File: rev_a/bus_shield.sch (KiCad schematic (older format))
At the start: 42 parts, among them J1 TERMINATE_JUMPER, SW1 MJTP1243, U1 74HCT08, U2 LM2940, U3 MCP2562, U4 LM117T-3.3, U5 ATMEGA328_DIP28, X1 16MHz

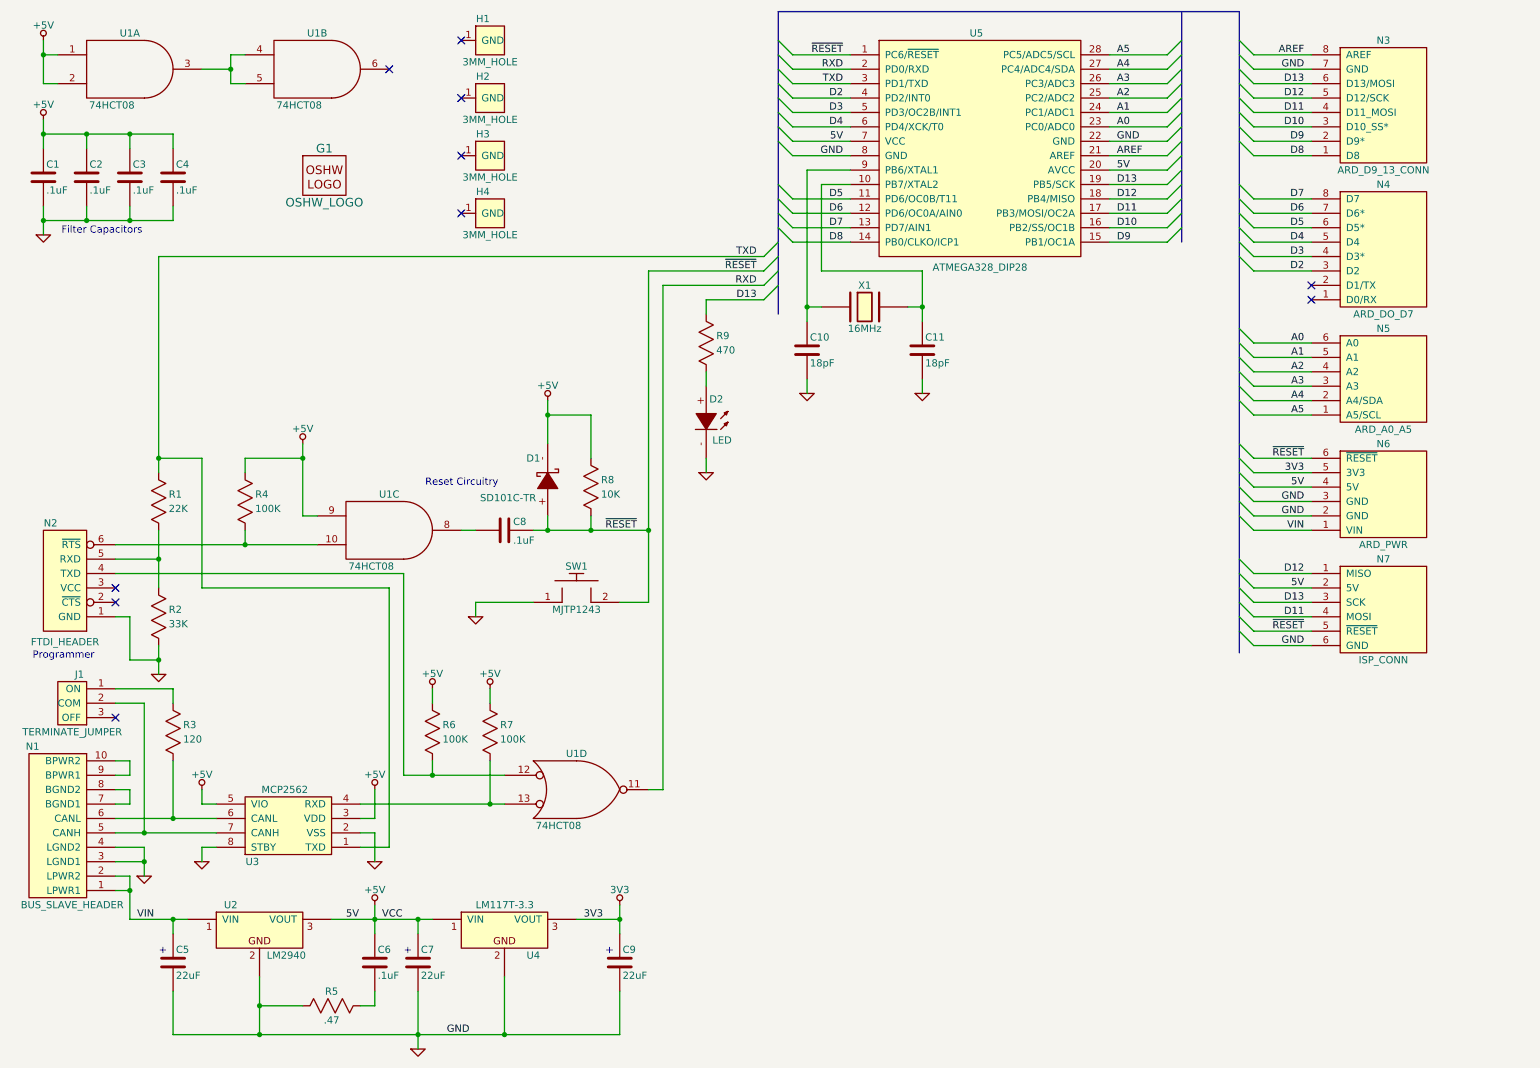
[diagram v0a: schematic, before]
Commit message: Reset from bus circuit.
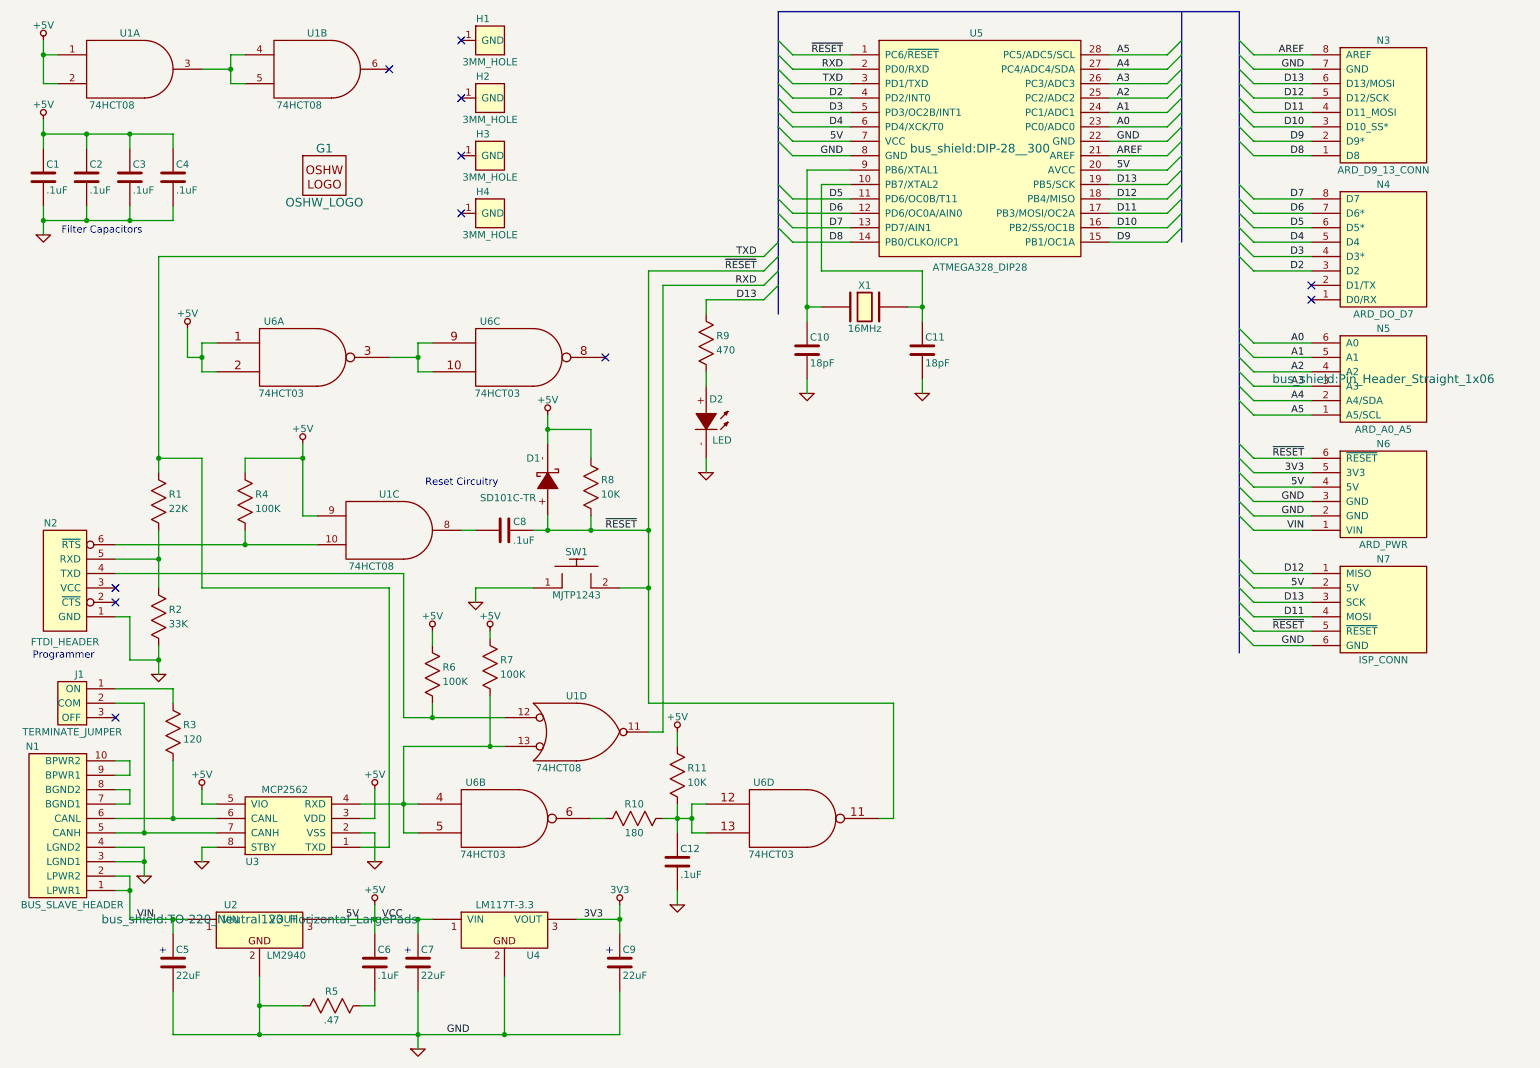
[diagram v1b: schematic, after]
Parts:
- added C12: .1uF, bus_shield:Capacitor3MMDiscRM2.5, symbol C_VERT
- added R10: 180, bus_shield:Resistor_Horizontal_400, symbol R_HORIZ
- added R11: 10K, bus_shield:Resistor_Horizontal_400, symbol R_VERT
- added U6: 74HCT03, bus_shield:DIP-14__300, symbol 74xx00
- N5: footprint ~ -> bus_shield:Pin_Header_Straight_1x06
- U2: footprint ~ -> bus_shield:TO-220_Neutral123_Horizontal_LargePads
- U5: footprint ~ -> bus_shield:DIP-28__300
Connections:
- net +5V: now also R11.2, U6.1, U6.14 (VCC), U6.14 (VCC), U6.14 (VCC), U6.14 (VCC), U6.2
- net GND: now also C12.2, U6.7 (GND), U6.7 (GND), U6.7 (GND), U6.7 (GND)
- net ~RESET: now also U6.11
- net at R7.1, U1.13, U3.4 (RXD): now also U6.4, U6.5
- new net: R10.1, U6.6
- new net: C12.1, R10.2, R11.1, U6.12, U6.13
- new net: U6.10, U6.3, U6.9
- no-connect marks 10 -> 11
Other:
- moved on the sheet: R6, R7, SW1, U1D

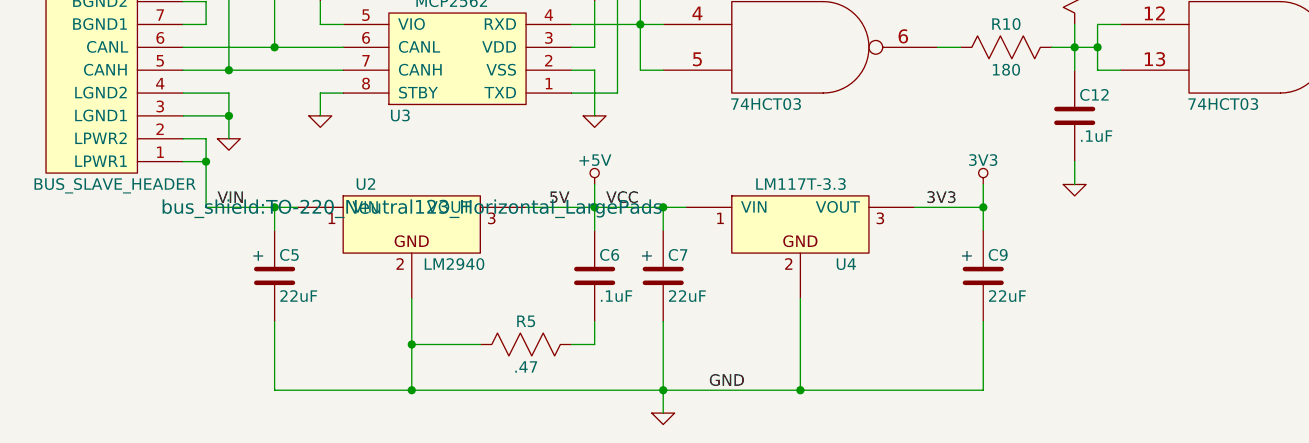
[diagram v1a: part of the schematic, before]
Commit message: Split 22uF capacitor into aluminum and tantalum.
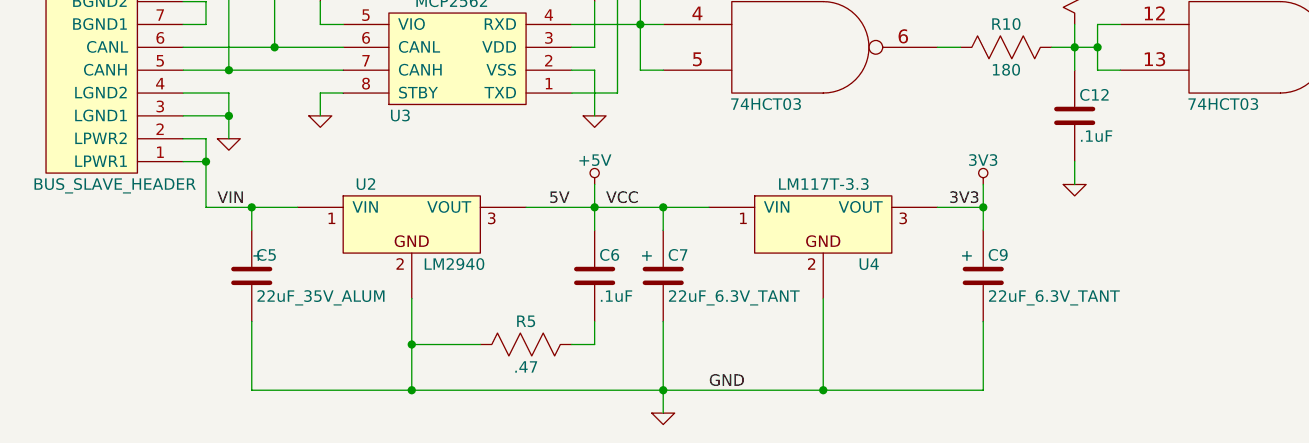
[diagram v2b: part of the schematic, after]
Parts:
- C5: value 22uF -> 22uF_35V_ALUM
- C7, C9: value 22uF -> 22uF_6.3V_TANT
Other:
- moved on the sheet: C5, U4
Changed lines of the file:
@@
 F 0 "U2" H 2000 7100 50  0000 C CNN
 F 1 "LM2940" H 2250 6750 50  0000 L CNN
-F 2 "bus_shield:TO-220_Neutral123_Horizontal_LargePads" H 2200 7000 60  0000 C CNN
+F 2 "bus_shield:TO-220_Neutral123_Horizontal_LargePads" H 2200 7000 60  0001 C CNN
 F 3 "" H 2200 7000 60  0000 C CNN
 	1    2200 6950
@@
 L C_VERT C5
 U 1 1 53EA3E9D
-P 1600 7200
-F 0 "C5" H 1620 7290 50  0000 L CNN
-F 1 "22uF" H 1620 7110 50  0000 L CNN
-F 2 "bus_shield:Capacitor3MMDiscRM2.5" H 1638 7050 30  0001 C CNN
-F 3 "" H 1600 7200 60  0000 C CNN
-	1    1600 7200
+P 1500 7200
+F 0 "C5" H 1520 7290 50  0000 L CNN
+F 1 "22uF_35V_ALUM" H 1520 7110 50  0000 L CNN
+F 2 "bus_shield:Capacitor3MMDiscRM2.5" H 1538 7050 30  0001 C CNN
+F 3 "" H 1500 7200 60  0000 C CNN
+	1    1500 7200
 	1    0    0    -1
 $EndComp
@@
 P 3300 7200
 F 0 "C7" H 3320 7290 50  0000 L CNN
-F 1 "22uF" H 3320 7110 50  0000 L CNN
+F 1 "22uF_6.3V_TANT" H 3320 7110 50  0000 L CNN
 F 2 "bus_shield:Capacitor3MMDiscRM2.5" H 3338 7050 30  0001 C CNN
 F 3 "" H 3300 7200 60  0000 C CNN
@@
 L VOLTAGE_REGULATOR U4
 U 1 1 54CE7224
-P 3900 6950
-F 0 "U4" H 4100 6750 50  0000 C CNN
-F 1 "LM117T-3.3" H 3700 7100 50  0000 L CNN
-F 2 "bus_shield:TO-220_Neutral123_Horizontal_LargePads" H 3900 7000 60  0001 C CNN
-F 3 "" H 3900 7000 60  0000 C CNN
-	1    3900 6950
+P 4000 6950
+F 0 "U4" H 4200 6750 50  0000 C CNN
+F 1 "LM117T-3.3" H 3800 7100 50  0000 L CNN
+F 2 "bus_shield:TO-220_Neutral123_Horizontal_LargePads" H 4000 7000 60  0001 C CNN
+F 3 "" H 4000 7000 60  0000 C CNN
+	1    4000 6950
 	1    0    0    -1
 $EndComp
@@
 P 4700 7200
 F 0 "C9" H 4720 7290 50  0000 L CNN
-F 1 "22uF" H 4720 7110 50  0000 L CNN
+F 1 "22uF_6.3V_TANT" H 4720 7110 50  0000 L CNN
 F 2 "bus_shield:Capacitor3MMDiscRM2.5" H 4738 7050 30  0001 C CNN
 F 3 "" H 4700 7200 60  0000 C CNN
@@
 	1    0    0    -1
 $EndComp
-Text Label 4450 6900 0    50   ~ 0
+Text Label 4550 6900 0    50   ~ 0
 3V3
 $Comp
@@
 $EndComp
 Wire Wire Line
-	1600 7700 1600 7400
+	1500 7700 1500 7400
 Connection ~ 2200 7500
 Wire Wire Line
@@
 	1400 6400 1400 6600
 Wire Wire Line
-	2700 6900 3400 6900
-Wire Wire Line
-	1600 7700 4700 7700
+	2700 6900 3500 6900
+Wire Wire Line
+	1500 7700 4700 7700
 Wire Wire Line
 	4200 3500 4500 3500
@@
 	1300 6900 1700 6900
 Wire Wire Line
-	1600 6900 1600 7000
-Connection ~ 1600 6900
+	1500 6900 1500 7000
+Connection ~ 1500 6900
 Connection ~ 3300 6900
 Wire Wire Line
-	4400 6900 4700 6900
+	4500 6900 4700 6900
 Wire Wire Line
 	4700 6800 4700 7000
@@
 	2200 7300 2200 7700
 Wire Wire Line
-	3900 7300 3900 7700
-Connection ~ 3900 7700
+	4000 7300 4000 7700
+Connection ~ 4000 7700
 Connection ~ 4700 6900
 Wire Wire Line
